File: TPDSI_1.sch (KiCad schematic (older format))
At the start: 18 parts, among them J1 Conn_01x02_Male, J2 Conn_01x02_Male, J7 Screw_Terminal_01x02, U3 MC7805_TO252-3(DPACK), U4 TLV2217_TO252-3

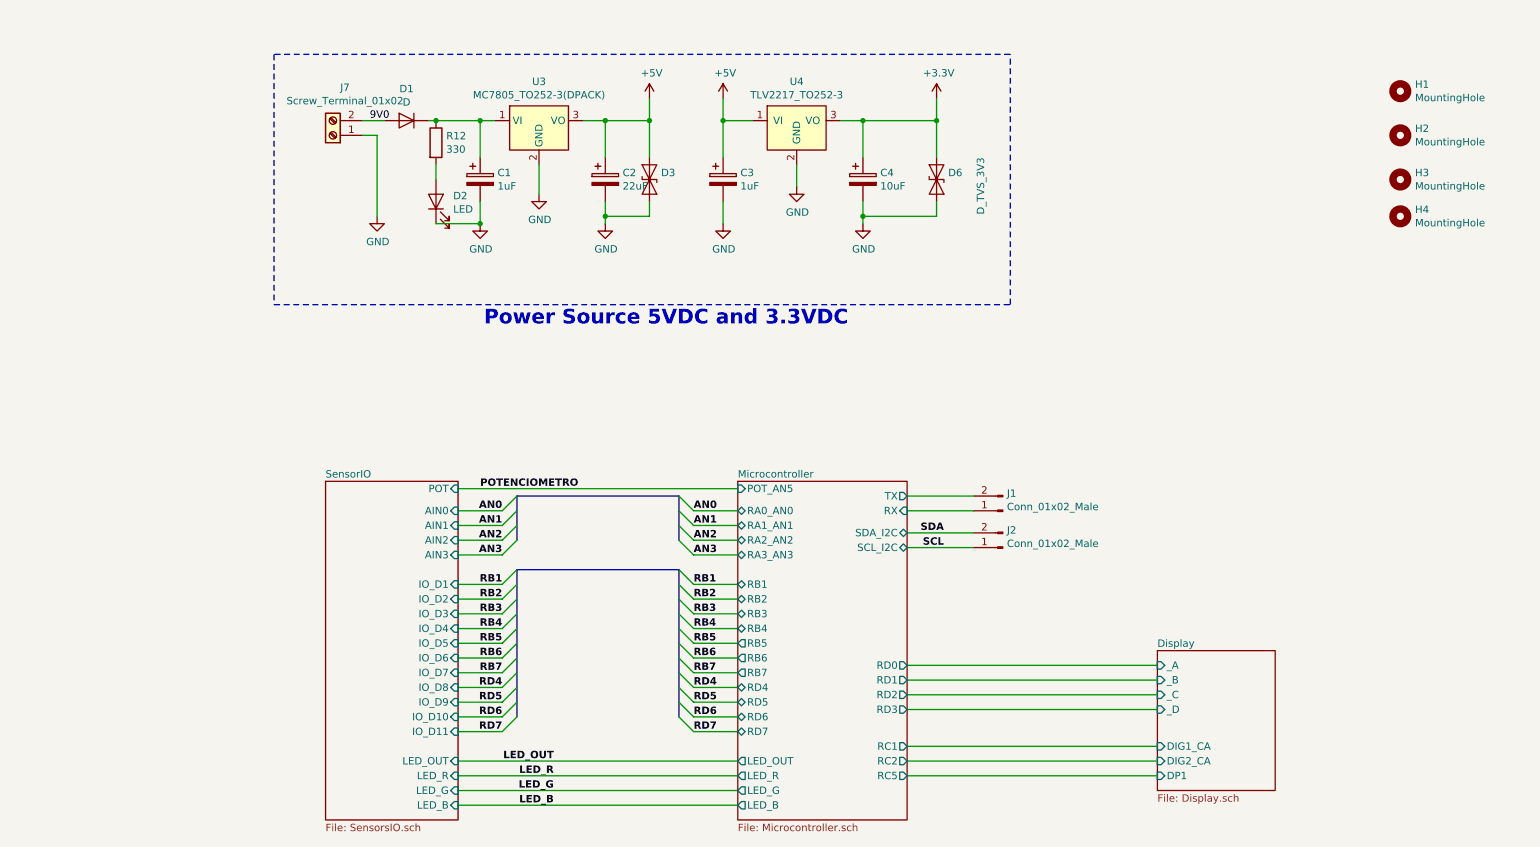
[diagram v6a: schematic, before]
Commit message: Se agrega info del circuito,prolijidad en conexiones  se corrije,ERC Warninsg no errores,pendinete Datasheet y algunos numeros de parte,Comentario esquematico1: no es necesario con los labels que esta considero que esta ok, componentes los dejo en 0603, grilla en pcb 0.127 mm a criterio propio, se colocan fiduciales, pendiente lo demas de PCB.
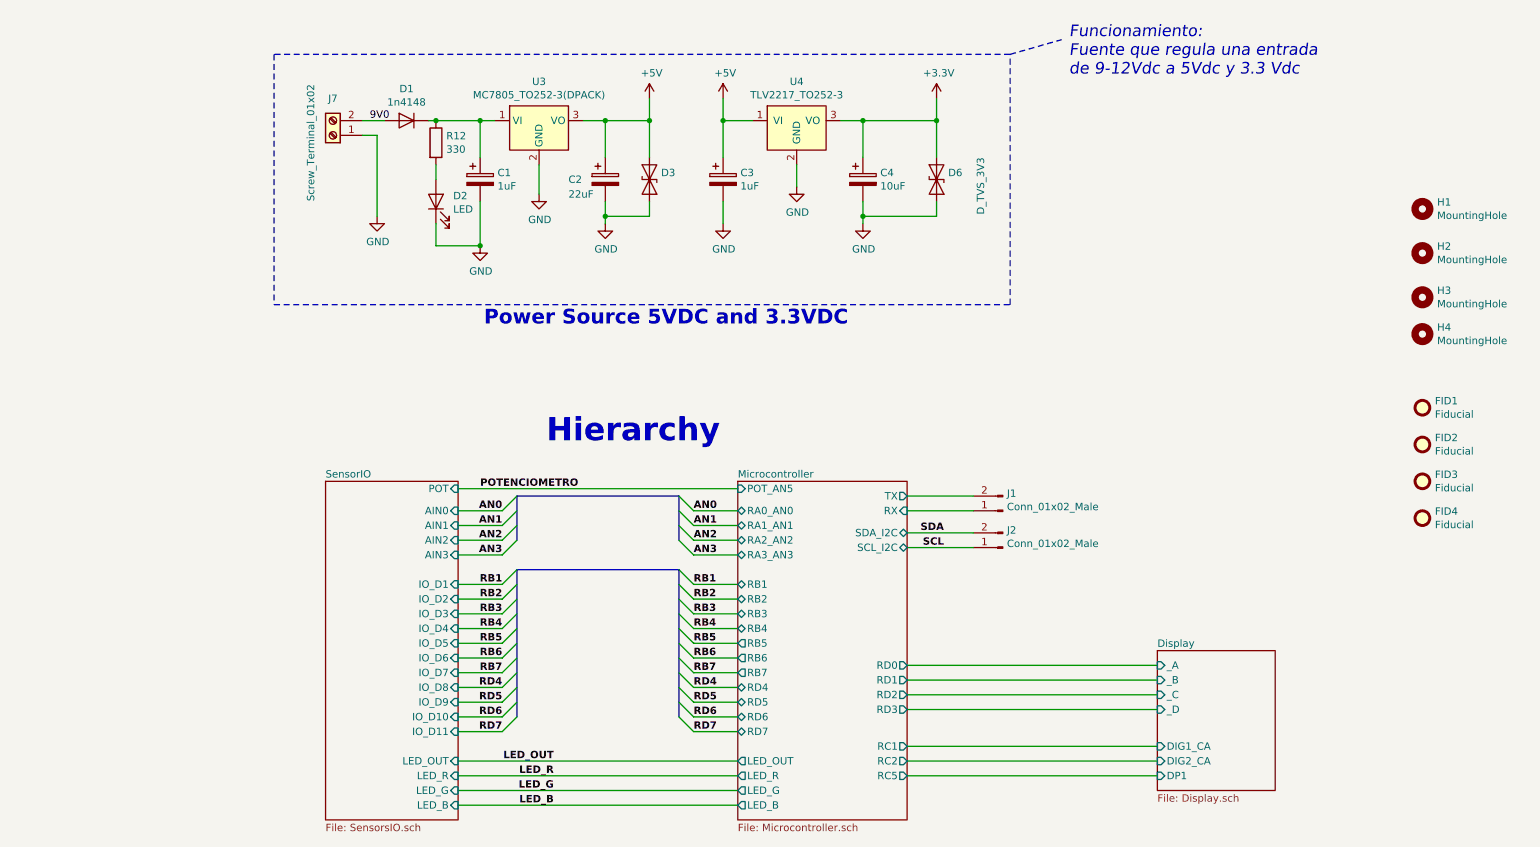
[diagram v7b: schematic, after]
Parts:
- added FID1, FID2, FID3, FID4: Fiducial, Fiducial:Fiducial_1mm_Mask2mm, symbol Mechanical:Fiducial
- D1: value D -> 1n4148
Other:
- note added: "Funcionamiento:\nFuente que regula una entrada\nde 9-12Vdc a 5Vdc y 3.3 Vdc"
- note added: "Hierarchy"
- moved on the sheet: H1, H2, H3, H4
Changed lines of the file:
@@
-$EndComp
-$Comp
-L Device:CP C?
-U 1 1 5CDBB843
-P 4650 1600
-AR Path="/5CCF7078/5CDBB843" Ref="C?"  Part="1"
-AR Path="/5CDBB843" Ref="C2"  Part="1"
-F 0 "C2" H 4768 1646 50  0000 L CNN
-F 1 "22uF" H 4768 1555 50  0000 L CNN
-F 2 "Capacitor_Tantalum_SMD:CP_EIA-7343-20_Kemet-V" H 4688 1450 50  0001 C CNN
-F 3 "~" H 4650 1600 50  0001 C CNN
-F 4 "P16517DKR-ND" H 4650 1600 50  0001 C CNN "Part Number"
-	1    4650 1600
-	1    0    0    -1
 $EndComp
 $Comp
@@
 L power:GND #PWR?
 U 1 1 5CDBB875
-P 3800 1900
+P 3800 2050
 AR Path="/5CCF7078/5CDBB875" Ref="#PWR?"  Part="1"
 AR Path="/5CDBB875" Ref="#PWR0104"  Part="1"
-F 0 "#PWR0104" H 3800 1650 50  0001 C CNN
-F 1 "GND" H 3805 1727 50  0000 C CNN
-F 2 "" H 3800 1900 50  0001 C CNN
-F 3 "" H 3800 1900 50  0001 C CNN
-	1    3800 1900
+F 0 "#PWR0104" H 3800 1800 50  0001 C CNN
+F 1 "GND" H 3805 1877 50  0000 C CNN
+F 2 "" H 3800 2050 50  0001 C CNN
+F 3 "" H 3800 2050 50  0001 C CNN
+	1    3800 2050
 	1    0    0    -1
 $EndComp
@@
 AR Path="/5CDBB896" Ref="D1"  Part="1"
 F 0 "D1" H 3300 1416 50  0000 C CNN
-F 1 "D" H 3300 1325 50  0000 C CNN
+F 1 "1n4148" H 3300 1325 50  0000 C CNN
 F 2 "Diode_SMD:D_SOD-123" H 3300 1200 50  0001 C CNN
 F 3 "~" H 3300 1200 50  0001 C CNN
@@
 Wire Wire Line
 	3450 1200 3500 1200
-Wire Wire Line
-	3800 1750 3800 1900
 Connection ~ 4650 1200
 Wire Wire Line
@@
 	3500 1600 3500 1500
 Wire Wire Line
-	3500 1900 3800 1900
-Connection ~ 3800 1900
+	3500 2050 3800 2050
+Connection ~ 3800 2050
 $Comp
 L Device:D_TVS D?
@@
 U 1 1 5CF6B993
 P 2800 1300
-F 0 "J7" H 2718 975 50  0000 C CNN
-F 1 "Screw_Terminal_01x02" H 2718 1066 50  0000 C CNN
+F 0 "J7" H 2800 1050 50  0000 C CNN
+F 1 "Screw_Terminal_01x02" V 2950 1350 50  0000 C CNN
 F 2 "TerminalBlock:TerminalBlock_bornier-2_P5.08mm" H 2800 1300 50  0001 C CNN
 F 3 "~" H 2800 1300 50  0001 C CNN
@@
 L Mechanical:MountingHole H1
 U 1 1 5CF85774
-P 10050 1000
-F 0 "H1" H 10150 1046 50  0000 L CNN
-F 1 "MountingHole" H 10150 955 50  0000 L CNN
-F 2 "MountingHole:MountingHole_3.2mm_M3" H 10050 1000 50  0001 C CNN
-F 3 "~" H 10050 1000 50  0001 C CNN
-	1    10050 1000
+P 10200 1800
+F 0 "H1" H 10300 1846 50  0000 L CNN
+F 1 "MountingHole" H 10300 1755 50  0000 L CNN
+F 2 "MountingHole:MountingHole_3.2mm_M3" H 10200 1800 50  0001 C CNN
+F 3 "~" H 10200 1800 50  0001 C CNN
+	1    10200 1800
 	1    0    0    -1
 $EndComp
@@
 L Mechanical:MountingHole H2
 U 1 1 5CF8F6CA
-P 10050 1300
-F 0 "H2" H 10150 1346 50  0000 L CNN
-F 1 "MountingHole" H 10150 1255 50  0000 L CNN
-F 2 "MountingHole:MountingHole_3.2mm_M3" H 10050 1300 50  0001 C CNN
-F 3 "~" H 10050 1300 50  0001 C CNN
-	1    10050 1300
+P 10200 2100
+F 0 "H2" H 10300 2146 50  0000 L CNN
+F 1 "MountingHole" H 10300 2055 50  0000 L CNN
+F 2 "MountingHole:MountingHole_3.2mm_M3" H 10200 2100 50  0001 C CNN
+F 3 "~" H 10200 2100 50  0001 C CNN
+	1    10200 2100
 	1    0    0    -1
 $EndComp
@@
 L Mechanical:MountingHole H3
 U 1 1 5CF918E9
-P 10050 1600
-F 0 "H3" H 10150 1646 50  0000 L CNN
-F 1 "MountingHole" H 10150 1555 50  0000 L CNN
-F 2 "MountingHole:MountingHole_3.2mm_M3" H 10050 1600 50  0001 C CNN
-F 3 "~" H 10050 1600 50  0001 C CNN
-	1    10050 1600
+P 10200 2400
+F 0 "H3" H 10300 2446 50  0000 L CNN
+F 1 "MountingHole" H 10300 2355 50  0000 L CNN
+F 2 "MountingHole:MountingHole_3.2mm_M3" H 10200 2400 50  0001 C CNN
+F 3 "~" H 10200 2400 50  0001 C CNN
+	1    10200 2400
 	1    0    0    -1
 $EndComp
@@
 L Mechanical:MountingHole H4
 U 1 1 5CF93C5D
-P 10050 1850
-F 0 "H4" H 10150 1896 50  0000 L CNN
-F 1 "MountingHole" H 10150 1805 50  0000 L CNN
-F 2 "MountingHole:MountingHole_3.2mm_M3" H 10050 1850 50  0001 C CNN
-F 3 "~" H 10050 1850 50  0001 C CNN
-	1    10050 1850
-	1    0    0    -1
-$EndComp
+P 10200 2650
+F 0 "H4" H 10300 2696 50  0000 L CNN
+F 1 "MountingHole" H 10300 2605 50  0000 L CNN
+F 2 "MountingHole:MountingHole_3.2mm_M3" H 10200 2650 50  0001 C CNN
+F 3 "~" H 10200 2650 50  0001 C CNN
+	1    10200 2650
+	1    0    0    -1
+$EndComp
+Text Notes 4250 3400 0    157  ~ 31
+Hierarchy
+Wire Wire Line
+	3800 1750 3800 2050
+Wire Wire Line
+	3500 2050 3500 1900
+$Comp
+L Device:CP C?
+U 1 1 5CDBB843
+P 4650 1600
+AR Path="/5CCF7078/5CDBB843" Ref="C?"  Part="1"
+AR Path="/5CDBB843" Ref="C2"  Part="1"
+F 0 "C2" H 4400 1600 50  0000 L CNN
+F 1 "22uF" H 4400 1500 50  0000 L CNN
+F 2 "Capacitor_Tantalum_SMD:CP_EIA-7343-20_Kemet-V" H 4688 1450 50  0001 C CNN
+F 3 "~" H 4650 1600 50  0001 C CNN
+F 4 "P16517DKR-ND" H 4650 1600 50  0001 C CNN "Part Number"
+	1    4650 1600
+	1    0    0    -1
+$EndComp
+Text Notes 7800 900  0    79   Italic 0
+Funcionamiento:\nFuente que regula una entrada\nde 9-12Vdc a 5Vdc y 3.3 Vdc
+Wire Notes Line
+	7400 750  7750 650
+$Comp
+L Mechanical:Fiducial FID1
+U 1 1 5D08E299
+P 10200 3150
+F 0 "FID1" H 10285 3196 50  0000 L CNN
+F 1 "Fiducial" H 10285 3105 50  0000 L CNN
+F 2 "Fiducial:Fiducial_1mm_Mask2mm" H 10200 3150 50  0001 C CNN
+F 3 "~" H 10200 3150 50  0001 C CNN
+	1    10200 3150
+	1    0    0    -1
+$EndComp
+$Comp
+L Mechanical:Fiducial FID2
+U 1 1 5D08EA59
+P 10200 3400
+F 0 "FID2" H 10285 3446 50  0000 L CNN
+F 1 "Fiducial" H 10285 3355 50  0000 L CNN
+F 2 "Fiducial:Fiducial_1mm_Mask2mm" H 10200 3400 50  0001 C CNN
+F 3 "~" H 10200 3400 50  0001 C CNN
+	1    10200 3400
+	1    0    0    -1
+$EndComp
+$Comp
+L Mechanical:Fiducial FID3
+U 1 1 5D08F11A
+P 10200 3650
+F 0 "FID3" H 10285 3696 50  0000 L CNN
+F 1 "Fiducial" H 10285 3605 50  0000 L CNN
+F 2 "Fiducial:Fiducial_1mm_Mask2mm" H 10200 3650 50  0001 C CNN
+F 3 "~" H 10200 3650 50  0001 C CNN
+	1    10200 3650
+	1    0    0    -1
+$EndComp
+$Comp
+L Mechanical:Fiducial FID4
+U 1 1 5D08F54B
+P 10200 3900
+F 0 "FID4" H 10285 3946 50  0000 L CNN
+F 1 "Fiducial" H 10285 3855 50  0000 L CNN
+F 2 "Fiducial:Fiducial_1mm_Mask2mm" H 10200 3900 50  0001 C CNN
+F 3 "~" H 10200 3900 50  0001 C CNN
+	1    10200 3900
+	1    0    0    -1
+$EndComp

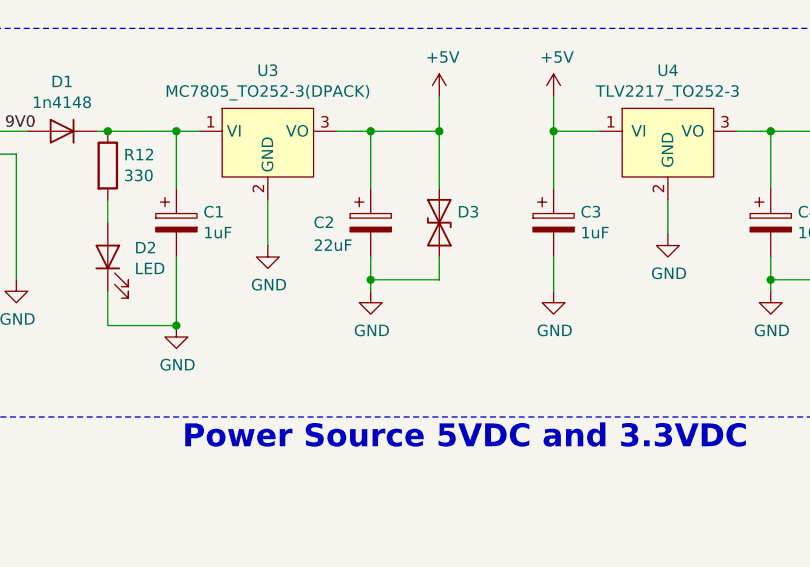
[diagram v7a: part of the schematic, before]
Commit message: Se agrega reglas de pcb , se corrige ERC en sch, se agrega grilla 0.127(5 mils) , se agrega plano de tierra, keep out para perforaciones, se agrega rotulo , se rutea pocas pistas
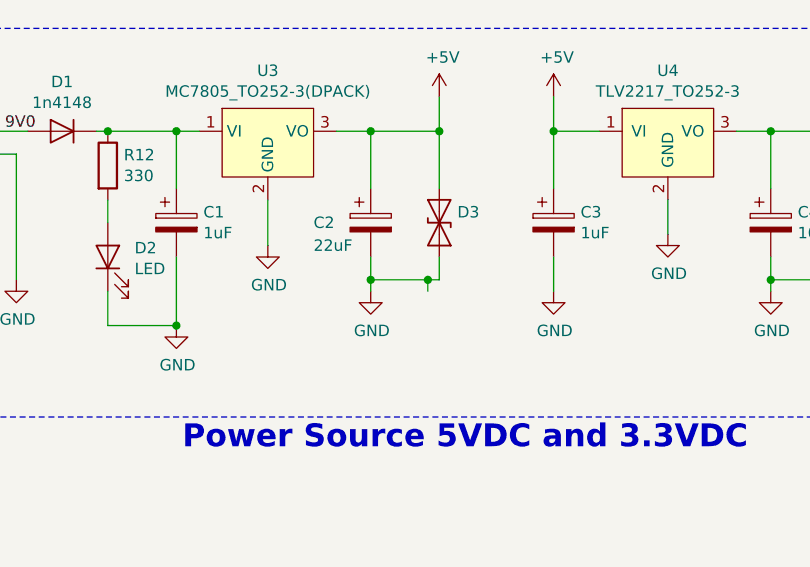
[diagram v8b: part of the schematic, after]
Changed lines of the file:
@@
 	4650 1900 4650 1850
-Wire Wire Line
-	4500 1200 4650 1200
 Wire Wire Line
 	4650 1200 4650 1450
@@
 F 3 "" H 5950 1650 50  0001 C CNN
 	1    5950 1650
-	1    0    0    -1
-$EndComp
-$Comp
-L power:GND #PWR?
-U 1 1 5CDBB888
-P 4200 1700
-AR Path="/5CCF7078/5CDBB888" Ref="#PWR?"  Part="1"
-AR Path="/5CDBB888" Ref="#PWR0106"  Part="1"
-F 0 "#PWR0106" H 4200 1450 50  0001 C CNN
-F 1 "GND" H 4205 1527 50  0000 C CNN
-F 2 "" H 4200 1700 50  0001 C CNN
-F 3 "" H 4200 1700 50  0001 C CNN
-	1    4200 1700
 	1    0    0    -1
 $EndComp
@@
 Connection ~ 4650 1200
 Wire Wire Line
-	4650 1200 4950 1200
-Wire Wire Line
 	4950 1450 4950 1200
 Connection ~ 4950 1200
@@
 	4950 1750 4950 1850
 Wire Wire Line
-	4950 1850 4650 1850
+	4950 1850 4900 1850
 Connection ~ 4650 1850
 Wire Wire Line
@@
 Wire Wire Line
 	6250 1200 6400 1200
-Wire Wire Line
-	6400 1200 6900 1200
 Connection ~ 6400 1200
 Wire Wire Line
@@
 	1    0    0    -1
 $EndComp
+Wire Wire Line
+	4900 1900 4900 1850
+Connection ~ 4900 1850
+Wire Wire Line
+	4900 1850 4650 1850
+Wire Wire Line
+	4500 1200 4650 1200
+Wire Wire Line
+	6400 1200 6900 1200
+Wire Wire Line
+	4650 1200 4950 1200
+$Comp
+L power:GND #PWR?
+U 1 1 5CDBB888
+P 4200 1700
+AR Path="/5CCF7078/5CDBB888" Ref="#PWR?"  Part="1"
+AR Path="/5CDBB888" Ref="#PWR0106"  Part="1"
+F 0 "#PWR0106" H 4200 1450 50  0001 C CNN
+F 1 "GND" H 4205 1527 50  0000 C CNN
+F 2 "" H 4200 1700 50  0001 C CNN
+F 3 "" H 4200 1700 50  0001 C CNN
+	1    4200 1700
+	1    0    0    -1
+$EndComp
